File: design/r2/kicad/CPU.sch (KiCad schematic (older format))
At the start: 11 parts, among them IC1 MC68010P10, Q2 5H8ET-10.000

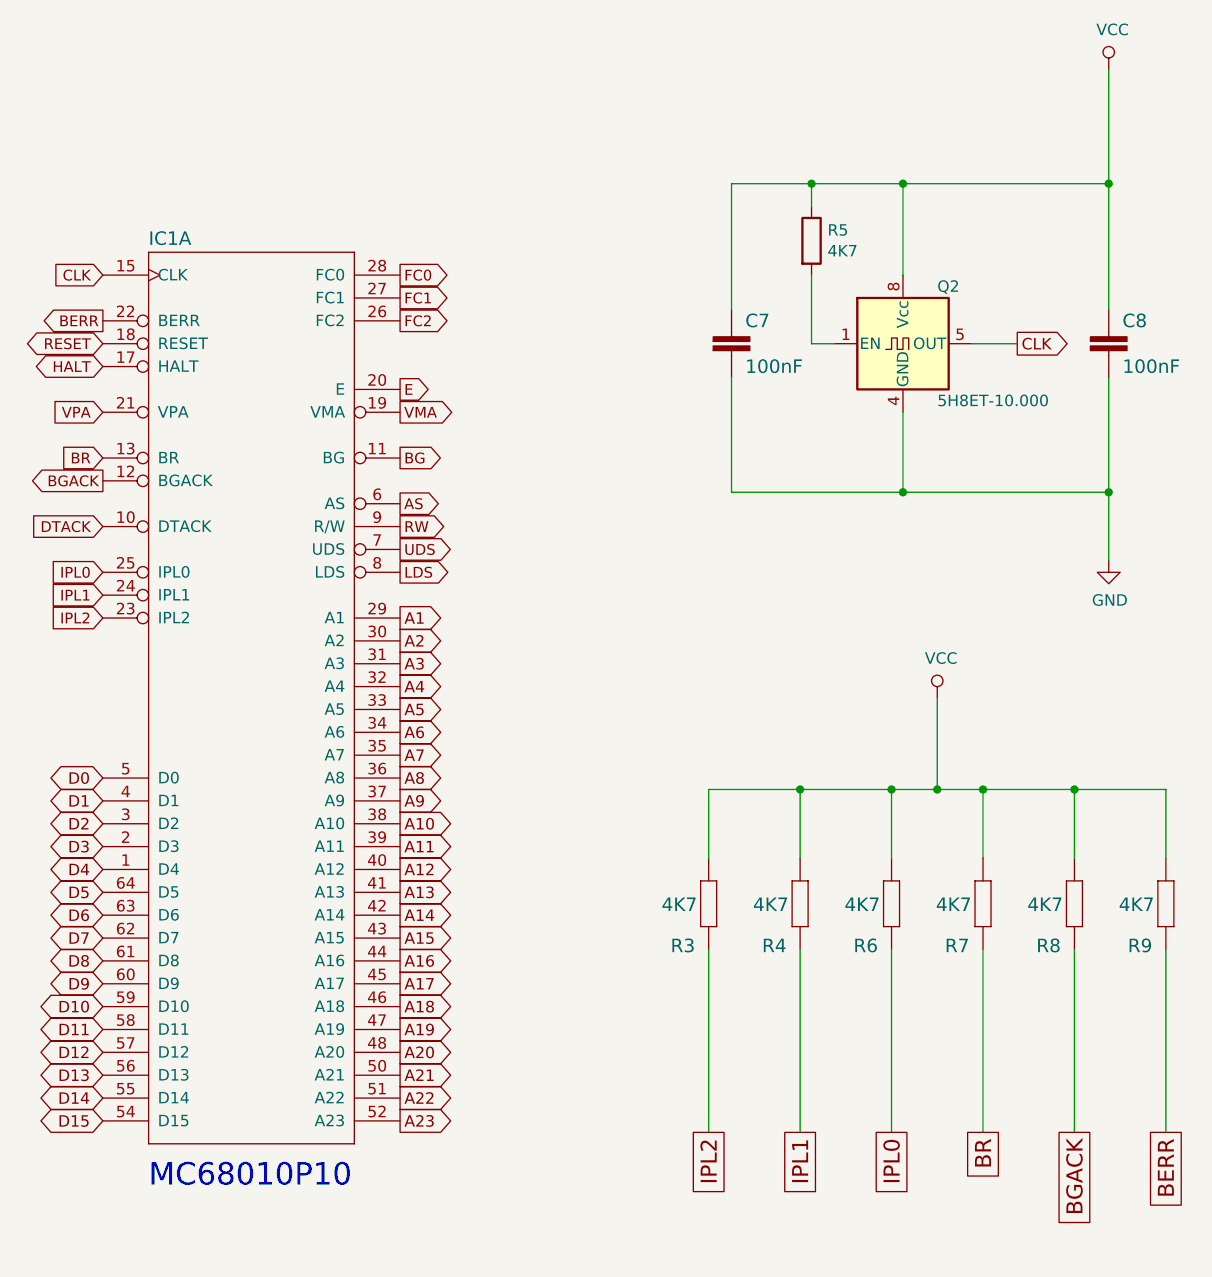
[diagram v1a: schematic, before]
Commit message: Schematic / GAL tweaks and do layout
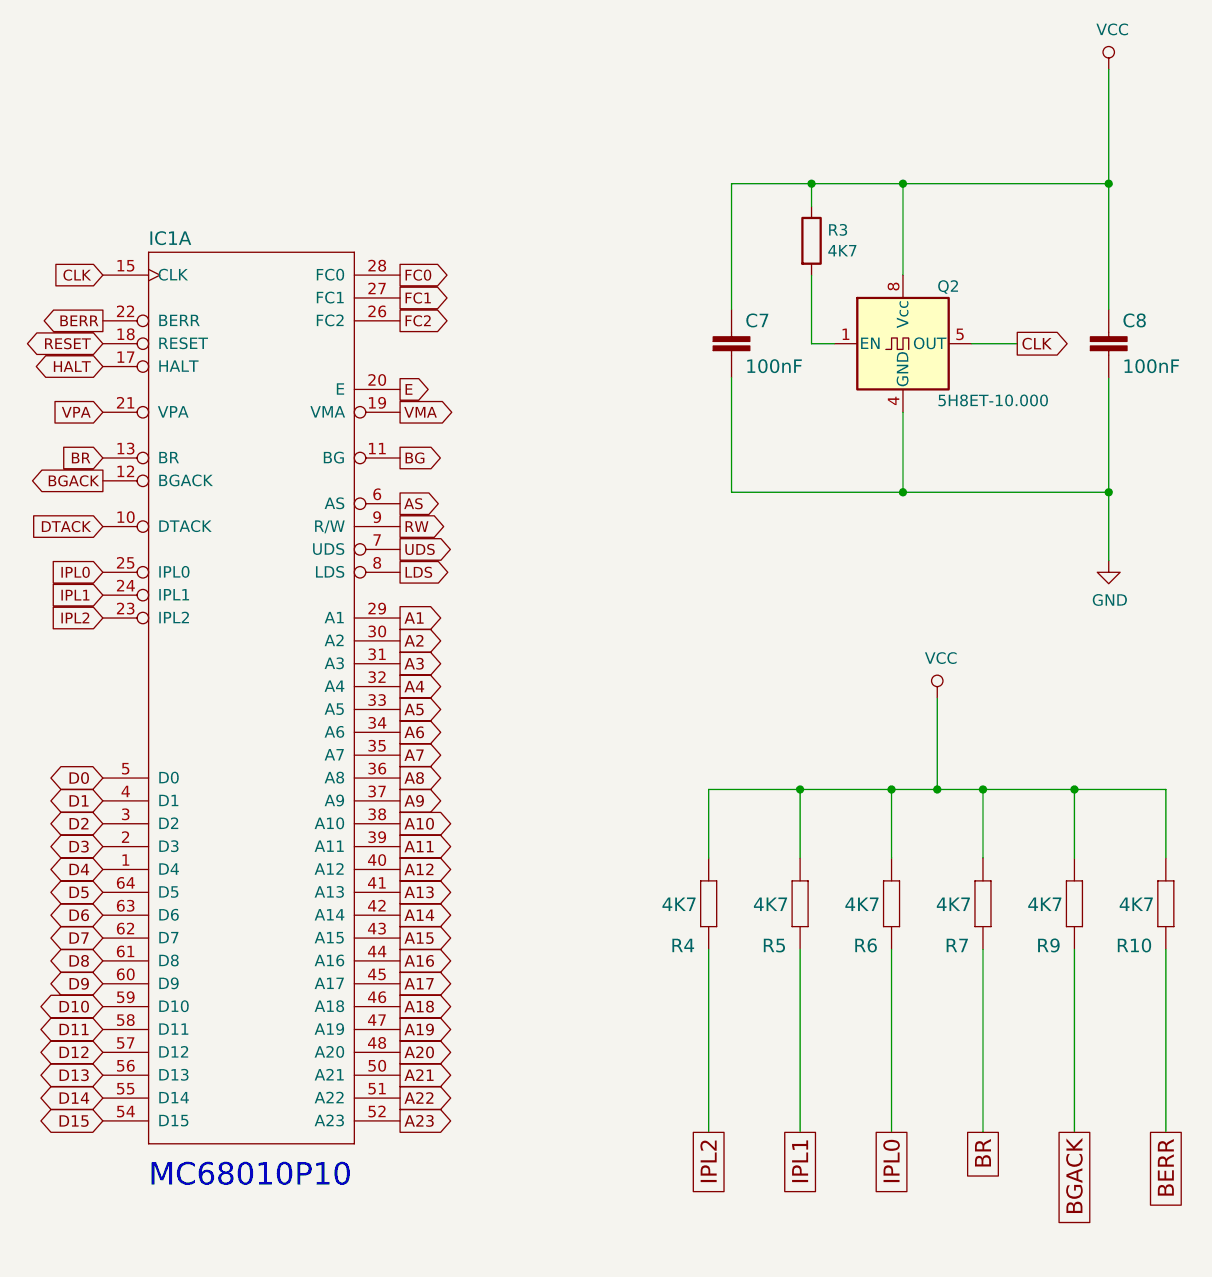
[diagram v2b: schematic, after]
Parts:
- renumbered R9 to R10, R5 to R3, R3 to R4, R4 to R5, R8 to R9
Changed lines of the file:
@@
 AR Path="/616E1A5C" Ref="R?"  Part="1"
 AR Path="/5E53B952/616E1A5C" Ref="R?"  Part="1"
-AR Path="/5E53B4B8/616E1A5C" Ref="R3"  Part="1"
-F 0 "R3" V 6250 4859 59  0000 L BNN
+AR Path="/5E53B4B8/616E1A5C" Ref="R4"  Part="1"
+F 0 "R4" V 6250 4859 59  0000 L BNN
 F 1 "4K7" V 6430 4850 59  0000 L BNN
 F 2 "rosco_m68k:0207_10" H 6400 4800 50  0001 C CNN
 F 3 "" H 6400 4800 50  0001 C CNN
 	1    6400 4800
-	0    -1   -1   0
-$EndComp
-$Comp
-L rosco_m68k-eagle-import:R-EU_0207_10 R?
-U 1 1 616E1A62
-P 6800 4800
-AR Path="/616E1A62" Ref="R?"  Part="1"
-AR Path="/5E53B952/616E1A62" Ref="R?"  Part="1"
-AR Path="/5E53B4B8/616E1A62" Ref="R4"  Part="1"
-F 0 "R4" V 6650 4859 59  0000 L BNN
-F 1 "4K7" V 6830 4850 59  0000 L BNN
-F 2 "rosco_m68k:0207_10" H 6800 4800 50  0001 C CNN
-F 3 "" H 6800 4800 50  0001 C CNN
-	1    6800 4800
 	0    -1   -1   0
 $EndComp
@@
 AR Path="/616E1A74" Ref="R?"  Part="1"
 AR Path="/5E53B952/616E1A74" Ref="R?"  Part="1"
-AR Path="/5E53B4B8/616E1A74" Ref="R8"  Part="1"
-F 0 "R8" V 7850 4859 59  0000 L BNN
+AR Path="/5E53B4B8/616E1A74" Ref="R9"  Part="1"
+F 0 "R9" V 7850 4859 59  0000 L BNN
 F 1 "4K7" V 8030 4850 59  0000 L BNN
 F 2 "rosco_m68k:0207_10" H 8000 4800 50  0001 C CNN
@@
 AR Path="/616E1A7A" Ref="R?"  Part="1"
 AR Path="/5E53B952/616E1A7A" Ref="R?"  Part="1"
-AR Path="/5E53B4B8/616E1A7A" Ref="R9"  Part="1"
-F 0 "R9" V 8250 4859 59  0000 L BNN
+AR Path="/5E53B4B8/616E1A7A" Ref="R10"  Part="1"
+F 0 "R10" V 8250 4859 59  0000 L BNN
 F 1 "4K7" V 8430 4850 59  0000 L BNN
 F 2 "rosco_m68k:0207_10" H 8400 4800 50  0001 C CNN
@@
 P 6850 1900
 AR Path="/5E53B952/616E1AB6" Ref="R?"  Part="1"
-AR Path="/5E53B4B8/616E1AB6" Ref="R5"  Part="1"
-F 0 "R5" H 6920 1946 50  0000 L CNN
+AR Path="/5E53B4B8/616E1AB6" Ref="R3"  Part="1"
+F 0 "R3" H 6920 1946 50  0000 L CNN
 F 1 "4K7" H 6920 1855 50  0000 L CNN
 F 2 "rosco_m68k:0207_10" V 6780 1900 50  0001 C CNN
@@
 Connection ~ 8150 1650
 Connection ~ 8150 3000
+$Comp
+L rosco_m68k-eagle-import:R-EU_0207_10 R?
+U 1 1 616E1A62
+P 6800 4800
+AR Path="/616E1A62" Ref="R?"  Part="1"
+AR Path="/5E53B952/616E1A62" Ref="R?"  Part="1"
+AR Path="/5E53B4B8/616E1A62" Ref="R5"  Part="1"
+F 0 "R5" V 6650 4859 59  0000 L BNN
+F 1 "4K7" V 6830 4850 59  0000 L BNN
+F 2 "rosco_m68k:0207_10" H 6800 4800 50  0001 C CNN
+F 3 "" H 6800 4800 50  0001 C CNN
+	1    6800 4800
+	0    -1   -1   0
+$EndComp
 $EndSCHEMATC

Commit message: Bite the bullet and do IPL properly...
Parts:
- removed R4, R5, R6: 4K7, rosco_m68k:0207_10, symbol rosco_m68k-eagle-import:R-EU_0207_10
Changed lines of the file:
@@
 Sheet 5 7
 Title "ROSCO_M68K GENERAL PURPOSE MC68010 COMPUTER"
-Date "2021-10-08"
-Rev "2.0"
+Date "2021-10-22"
+Rev "2.1"
 Comp "The Really Old-School Company Limited"
 Comment1 "OSHWA UK000006 (https://certification.oshwa.org/uk000006.html)"
@@
 D15
 Wire Wire Line
-	7400 4300 7200 4300
-Wire Wire Line
-	7200 4300 6800 4300
-Wire Wire Line
-	6800 4300 6400 4300
-Wire Wire Line
-	6400 4300 6400 4600
-Wire Wire Line
 	7400 4300 7600 4300
 Wire Wire Line
@@
 Wire Wire Line
 	7600 4600 7600 4300
-Wire Wire Line
-	7200 4600 7200 4300
-Wire Wire Line
-	6800 4600 6800 4300
-Connection ~ 7400 4300
 Connection ~ 8000 4300
 Connection ~ 7600 4300
-Connection ~ 7200 4300
-Connection ~ 6800 4300
-Wire Wire Line
-	6400 5800 6400 5000
-Wire Wire Line
-	6800 5800 6800 5000
-Text GLabel 6800 5800 3    70   UnSpc ~ 0
-IPL1
-Wire Wire Line
-	7200 5800 7200 5000
-Text GLabel 7200 5800 3    70   UnSpc ~ 0
-IPL0
 Wire Wire Line
 	8000 5800 8000 5000
@@
 Text GLabel 8400 5800 3    70   UnSpc ~ 0
 BERR
-$Comp
-L rosco_m68k-eagle-import:R-EU_0207_10 R?
-U 1 1 616E1A5C
-P 6400 4800
-AR Path="/616E1A5C" Ref="R?"  Part="1"
-AR Path="/5E53B952/616E1A5C" Ref="R?"  Part="1"
-AR Path="/5E53B4B8/616E1A5C" Ref="R4"  Part="1"
-F 0 "R4" V 6250 4859 59  0000 L BNN
-F 1 "4K7" V 6430 4850 59  0000 L BNN
-F 2 "rosco_m68k:0207_10" H 6400 4800 50  0001 C CNN
-F 3 "" H 6400 4800 50  0001 C CNN
-	1    6400 4800
-	0    -1   -1   0
-$EndComp
-$Comp
-L rosco_m68k-eagle-import:R-EU_0207_10 R?
-U 1 1 616E1A68
-P 7200 4800
-AR Path="/616E1A68" Ref="R?"  Part="1"
-AR Path="/5E53B952/616E1A68" Ref="R?"  Part="1"
-AR Path="/5E53B4B8/616E1A68" Ref="R6"  Part="1"
-F 0 "R6" V 7050 4859 59  0000 L BNN
-F 1 "4K7" V 7230 4850 59  0000 L BNN
-F 2 "rosco_m68k:0207_10" H 7200 4800 50  0001 C CNN
-F 3 "" H 7200 4800 50  0001 C CNN
-	1    7200 4800
-	0    -1   -1   0
-$EndComp
 $Comp
 L rosco_m68k-eagle-import:R-EU_0207_10 R?
@@
 Wire Wire Line
 	7400 3900 7400 4300
-Text GLabel 6400 5800 3    70   UnSpc ~ 0
-IPL2
 Text GLabel 7750 2350 2    50   Output ~ 0
 CLK
@@
 Connection ~ 8150 1650
 Connection ~ 8150 3000
-$Comp
-L rosco_m68k-eagle-import:R-EU_0207_10 R?
-U 1 1 616E1A62
-P 6800 4800
-AR Path="/616E1A62" Ref="R?"  Part="1"
-AR Path="/5E53B952/616E1A62" Ref="R?"  Part="1"
-AR Path="/5E53B4B8/616E1A62" Ref="R5"  Part="1"
-F 0 "R5" V 6650 4859 59  0000 L BNN
-F 1 "4K7" V 6830 4850 59  0000 L BNN
-F 2 "rosco_m68k:0207_10" H 6800 4800 50  0001 C CNN
-F 3 "" H 6800 4800 50  0001 C CNN
-	1    6800 4800
-	0    -1   -1   0
-$EndComp
 $EndSCHEMATC
